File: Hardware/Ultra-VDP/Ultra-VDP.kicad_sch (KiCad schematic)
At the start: 70 parts, among them J1 BC075-05, J2 BC075-10, J3 CBUS, J4 BC075-10, J5 BC075-06, J6 BC075-10, J7 BC075-10, J8 BC075-05, U14 V53C8125HT30, U3 V9958, U6 LMH1980, Y1 21.477270MHz, Y3 4.433618MHz

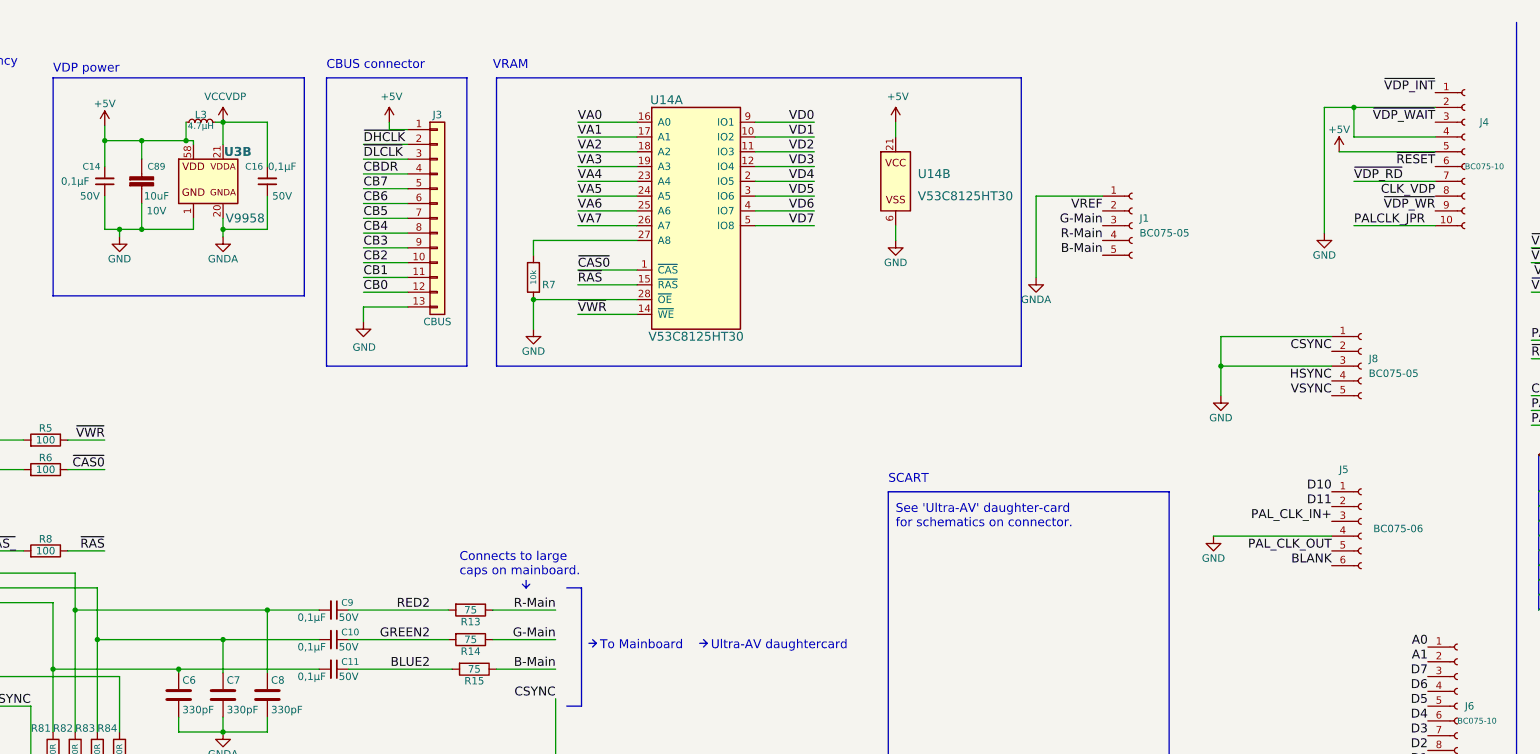
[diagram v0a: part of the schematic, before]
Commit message: Finished the VDP-board, finished up the mixer-section, removed the buffer-pins from the FPGA, and instead added external buffers for the slots, designed a marquee-block with the Ultra-MSX logo, designed the logotype, andmultiple other changes.
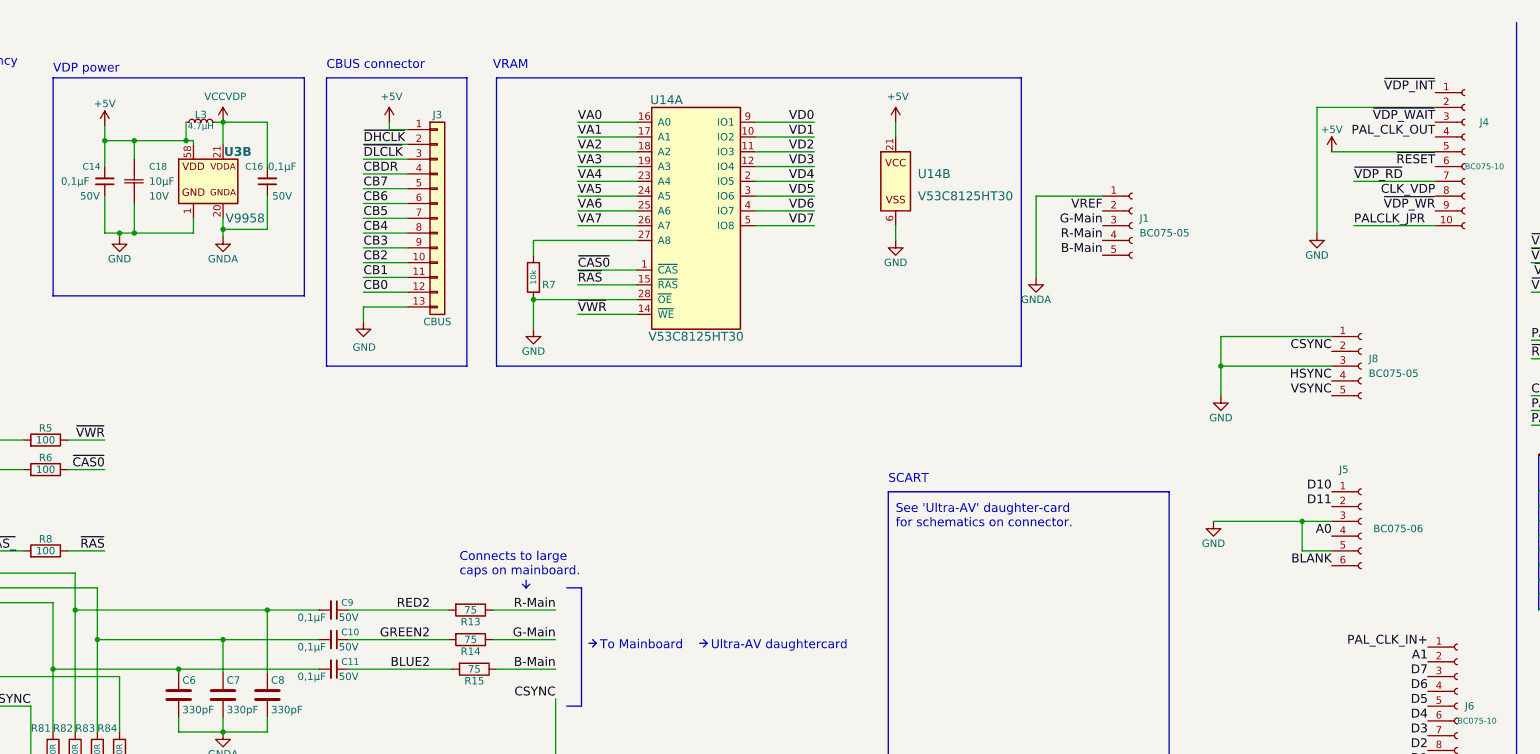
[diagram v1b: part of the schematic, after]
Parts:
- removed C89: C_GRM21BR71A106KA73K, Capacitor_SMD:C_0805_2012Metric_Pad1.18x1.45mm_HandSolder, symbol LRJ-parts:C_GRM21BR71A106KA73K
- added C18: C_GRM188D71A106KA73D, Capacitor_SMD:C_0603_1608Metric, symbol LRJ-parts:C_GRM188D71A106KA73D
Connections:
- net +5V: now also C18.1
- net A0: now also J5.4 (Pin_4); no longer J6.1 (Pin_1)
- net GND: now also J5.3 (Pin_3), J5.5 (Pin_5), C18.2; no longer J4.4 (Pin_4), J5.4 (Pin_4)
- net PAL_CLK_IN+: now also J6.1 (Pin_1); no longer J5.3 (Pin_3)
- net PAL_CLK_OUT: now also J4.4 (Pin_4); no longer J5.5 (Pin_5)

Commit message: Redesigned VDP-board to include a socket, increased it to 4 layers. Various clean-ups here and there. Improved the printer-port and joystick-port 3D-models. Improved the cooling-fin 3D-model, and added attachment-spring in 3D-model.
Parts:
- removed C3: 0.1uF, Capacitor_SMD:C_0603_1608Metric, symbol Device:C
- added C19: 47pF, Capacitor_SMD:C_0603_1608Metric, symbol Device:C
- added C3: C_CL21B223KBANFNC, Capacitor_SMD:C_0805_2012Metric_Pad1.18x1.45mm_HandSolder, symbol LRJ-parts:C_CL21B223KBANFNC
- added L1: L_MLZ2012M4R7HT000, Inductor_SMD:L_0805_2012Metric, symbol LRJ-parts:L_MLZ2012M4R7HT000
- added R10: 75, Resistor_SMD:R_0603_1608Metric, symbol Device:R
- added R12: 100, Resistor_SMD:R_0603_1608Metric, symbol Device:R
- U3: footprint Ultra-MSX:IC_SDIP64_600 -> Ultra-MSX:DIP-64_W19.05mm_SMDSocket_SmallPads
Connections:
- net +5V: now also R20.1, L1.1; no longer C17.1, C73.1, R20.2, R60.2, U6.3 (VCC)
- net COMPSYNC: now also R10.1, R12.2; no longer C12.1, C15.2
- net GND: now also C19.2, C3.2, R10.2
- net VCCVDP: now also R60.2
- net ~{VDP_INT}: now also R20.2; no longer R20.1
- net HORSYNC: now reaches R84.1, U3.5 (HSYNC)
- net PALCLK_JPR renamed NTSC_CLKO
- new net: C12.1, C15.2, C19.1, R12.1
- new net: C3.1, U3.33 (VBB)
- new net +5V_SYNC: C17.1, C73.1, L1.2, U6.3 (VCC)
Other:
- note added: "1. Video Display Processor (VDP)"
- note added: "1.1. VDP power"
- note added: "1.2. CBUS connector"
- note added: "1/6 of Crystal Frequency (3,579545 MHz, aka NTSC)"
- note added: "2. VRAM"
- note added: "DisplayPort has a mode where it sends raw RGB down the wire, meaning a DP to VGA converter is "just" a DAC and maybe a presence detection EEPROM. Example-chip:"
- note added: "From the MSX-Engine (see Mainboard)"
- note added: "PCB Layout Notes: DIP-64 socket - Mill-Max 117-43-764-41-105000"
- note added: "VGA clocks: ------------- 640x400 (70Hz) - 25.175 MHz 640x480 (60Hz) - 25.175 MHz Pal clocks: ------------- 704x576 (50Hz) - 4.43361875 MHz NTSC clocks: -------------- 704x480 (60Hz) - 3.579545 MHz"
- note removed: "1/6 of Crystal Frequency (3,579545 MHz)"
- note removed: "CBUS connector"
- note removed: "DisplayPort has a mode where it sends raw RGB down the wire, meaning a DP to VGA converter is "just" a DAC and maybe a presence detection EEPROM. Example-chip: PTN3356R1BSMP"
- note removed: "PCB Layout Notes: Keep trace length between AD723 and 75 ohm resistors to minimum AD723 bypass capacitors: VCC1(12), VREF(14) -> GND1(1), VCC2(19) -> GND2(24)"
- note removed: "VCC_ROM"
- note removed: "VDP power"
- note removed: "VRAM"
- moved on the sheet: C1, C10, C11, C12, C13, C14, C15, C16, C17, C18, C2, C4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

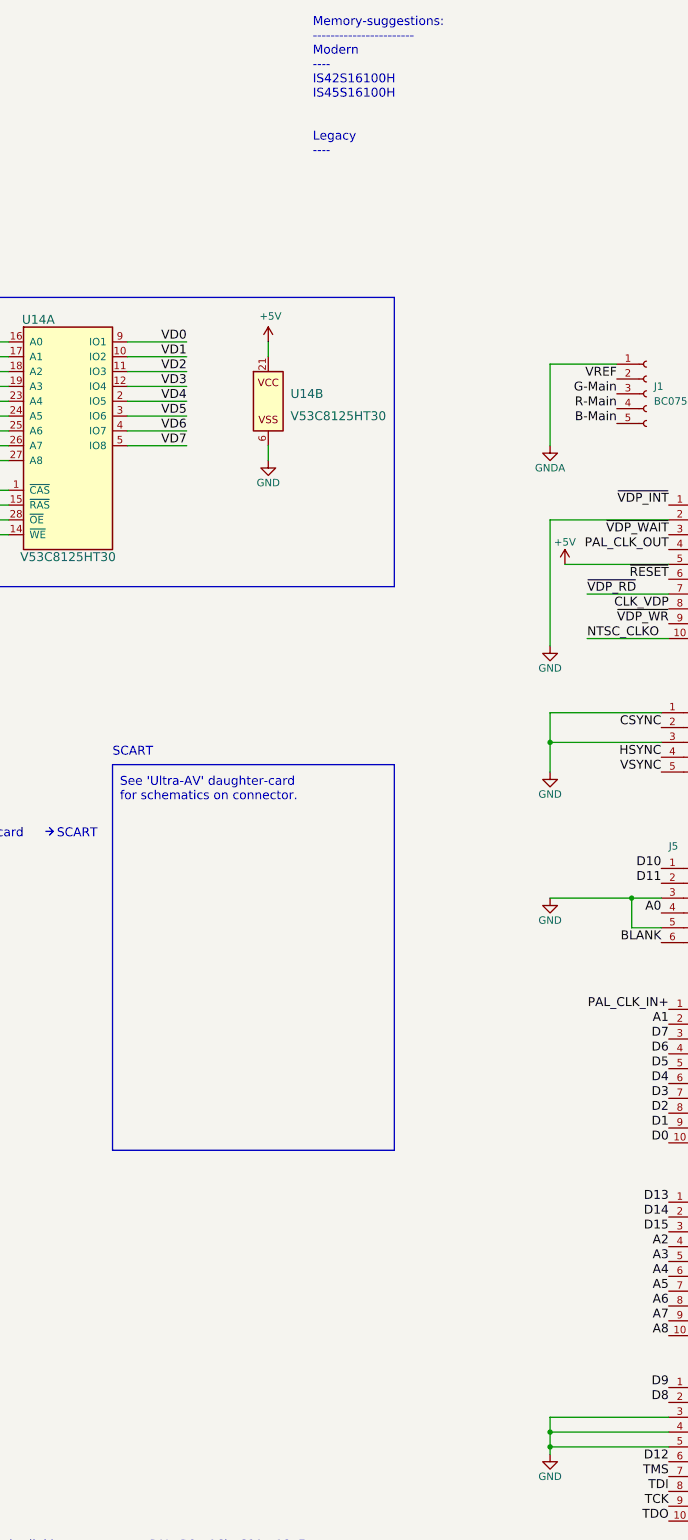
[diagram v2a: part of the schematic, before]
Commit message: Generated first PDF-files
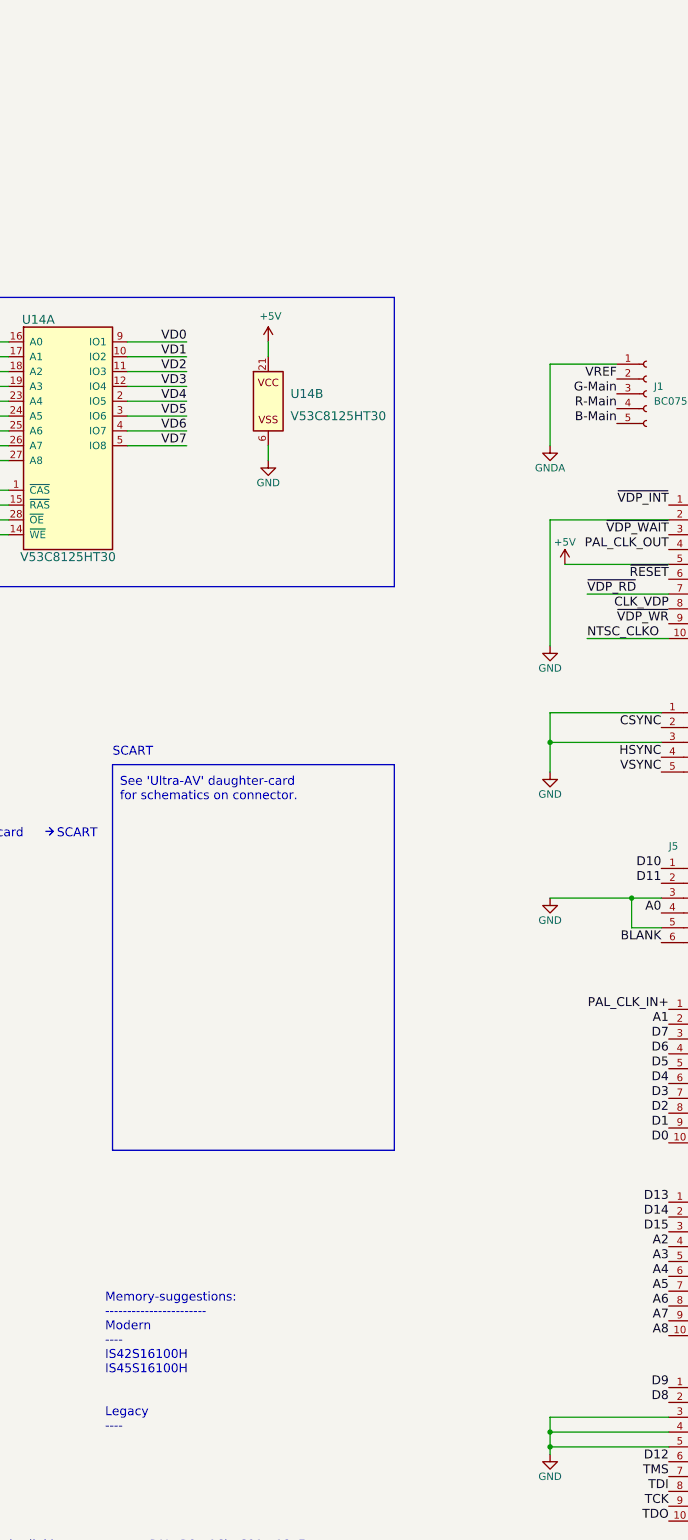
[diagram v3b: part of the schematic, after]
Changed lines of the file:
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@@
   )
   (text "Memory-suggestions:\n-----------------------\nModern\n----\nIS42S16100H\nIS45S16100H\n\n\nLegacy\n----"
-    (at 299.72 -5.08 0)
+    (at 264.16 213.36 0)
     (effects (font (size 1.524 1.524)) (justify left bottom))
   )

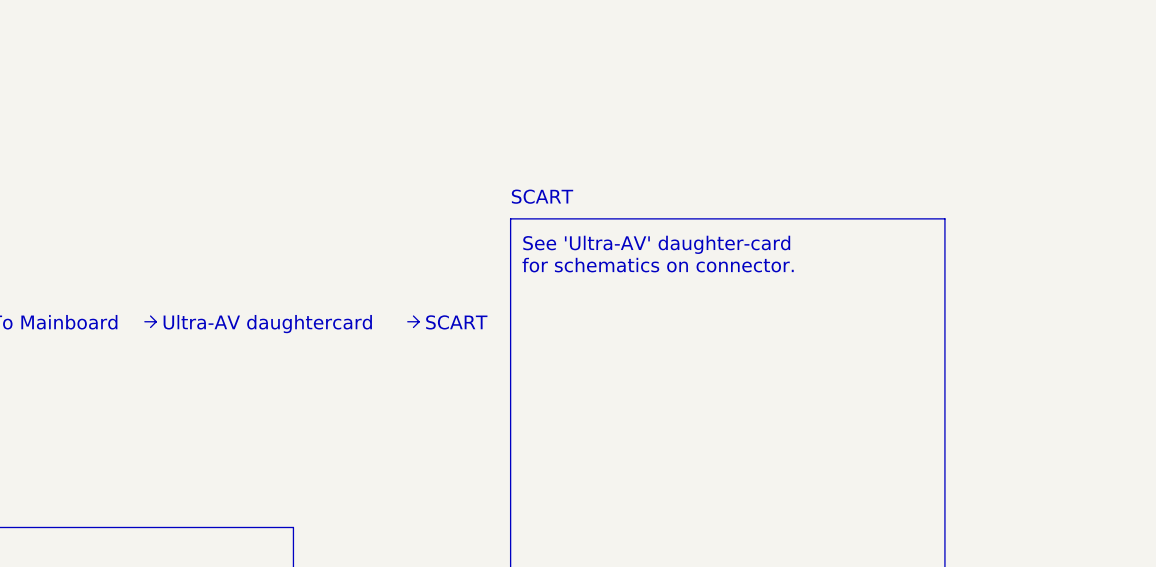
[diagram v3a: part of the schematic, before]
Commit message: Started remodelling the MSX cart-shells, as they don't seem to fit the cartridge-pcb's. Bit of clean-up in the directories.
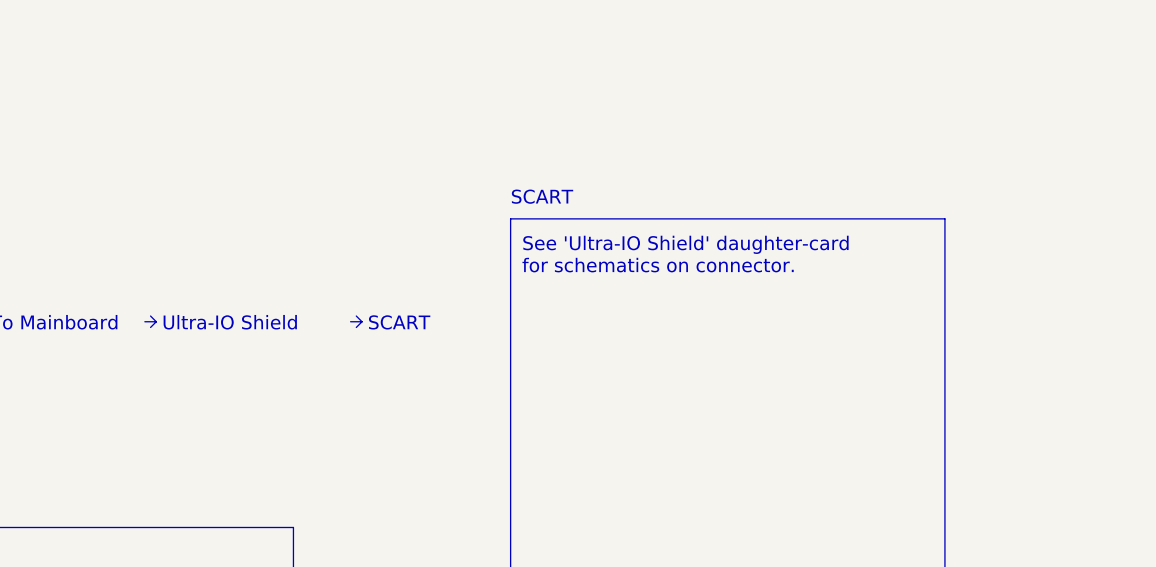
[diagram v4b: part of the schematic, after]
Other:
- note added: "See 'Ultra-IO Shield' daughter-card for schematics on connector."
- note added: "Ultra-IO Shield"
- note removed: "See 'Ultra-AV' daughter-card for schematics on connector."
- note removed: "Ultra-AV daughtercard"
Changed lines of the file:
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@@
     (stroke (width 0) (type default) (color 0 0 0 0))
   )
-  (polyline (pts (xy 254 110.49) (xy 255.27 110.49))
+  (polyline (pts (xy 247.65 110.49) (xy 248.92 110.49))
     (stroke (width 0) (type solid) (color 0 0 0 0))
   )
@@
     (stroke (width 0) (type default) (color 0 0 0 0))
   )
-  (polyline (pts (xy 254.635 111.125) (xy 255.27 110.49))
+  (polyline (pts (xy 248.285 111.125) (xy 248.92 110.49))
     (stroke (width 0) (type solid) (color 0 0 0 0))
   )
@@
     (stroke (width 0) (type default) (color 0 0 0 0))
   )
-  (polyline (pts (xy 254.635 109.855) (xy 255.27 110.49))
+  (polyline (pts (xy 248.285 109.855) (xy 248.92 110.49))
     (stroke (width 0) (type solid) (color 0 0 0 0))
   )
@@
     (effects (font (size 1.524 1.524)) (justify left bottom))
   )
-  (text "See 'Ultra-AV' daughter-card \nfor schematics on connector."
+  (text "See 'Ultra-IO Shield' daughter-card \nfor schematics on connector."
     (at 266.7 105.41 0)
     (effects (font (size 1.524 1.524)) (justify left bottom))
@@
     (effects (font (size 1.524 1.524)) (justify left bottom))
   )
-  (text "Ultra-AV daughtercard\n" (at 226.695 111.76 0)
+  (text "Ultra-IO Shield\n" (at 226.695 111.76 0)
     (effects (font (size 1.524 1.524)) (justify left bottom))
   )
@@
     (effects (font (size 1.524 1.524)) (justify left bottom))
   )
-  (text "SCART\n" (at 255.905 111.76 0)
+  (text "SCART\n" (at 249.555 111.76 0)
     (effects (font (size 1.524 1.524)) (justify left bottom))
   )

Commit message: Started fixing many small issues.
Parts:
- added trace1, trace10, trace11, trace12, trace13, trace14, trace15, trace16, trace17, trace18, trace19, trace2, trace20, trace21, trace3, trace4, trace5, trace6, trace7, trace8, trace9: pcb-trace, LRJ:NetTie-2_SMD_Pad0.2mm, symbol LRJ-parts:Trace
- C10, C11, C14, C15, C16, C17, C9: Mounting Type SMD -> (none); Mounting type (none) -> SMD; Voltage Rating (none) -> 50V; Voltage Rating  50V -> (none)
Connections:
- net GNDA is gone; now on net GND: C16.1, C6.2, C7.2, C8.2, J1.1 (Pin_1), R81.2, R82.2, R83.2, U3.20 (GNDA)
- net +5V: now also C73.1
- net A2: now also trace5.2
- net A3: now also trace6.2
- net A4: now also trace7.2
- net A5: now also trace8.2
- net A6: now also trace9.2
- net A7: now also trace10.2
- net A8: now also trace11.2
- net BLANK: now also trace21.1; no longer J5.6 (Pin_6)
- net D10: now also trace19.1
- net D11: now also trace20.1
- net D12: now also trace14.2
- net D13: now also trace1.2
- net D14: now also trace3.2
- net D15: now also trace4.2
- net D8: now also trace13.2
- net D9: now also trace12.2
- net TCK: now also trace17.2
- net TDI: now also trace16.2
- net TDO: now also trace18.2
- net TMS: now also trace15.2
- net VREF: now also trace2.2
- net +5V_SYNC renamed VDDSYNC
- net VDDSYNC: no longer C73.1
- new net: J5.6 (Pin_6), trace21.2
- no-connect marks 3 -> 24
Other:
- note added: "2. Video Random Access Memory (VRAM)"
- note added: "3. Sync Separator"
- note added: "3.1. Sync Separator power"
- note added: "4. PAL Clock Generator"
- note added: "4.1. Region Selection"
- note added: "5. SCART Connector"
- note added: "6. Motherboard connectors"
- note added: "Addressing"
- note added: "CLOCK signals"
- note added: "CONTROL signals"
- note added: "DATA bus"
- note added: "JP4, JP5: 1-2: NTSC; 2-3: PAL (Use a wire link)"
- note added: "Note: these pins are only in use when utilizing a more advanced VDP such as V9990, or F18A. ->"
- note added: "To Motherboard"
- note added: "VIDEO signals"
- note added: "up to: 56 pins. But we can shave it down to 51... Potential sockets: Amphenol FCI MDT350M01001VT (M.2) Samtec PCIE-LP-04-01-F-DV-A-TR (PCIe x4)"
- note removed: "2. VRAM"
- note removed: "JP3, JP4: 1-2: V9938; 2-3: V9958 (Use a wire link) JP4, JP5: 1-2: NTSC; 2-3: PAL (Use a wire link)"
- note removed: "PAL Clock Generator"
- note removed: "Sync Separator power"
- note removed: "To Mainboard"
- title: (none) -> Ultra-VDP
- moved on the sheet: C1, C10, C11, C12, C13, C14, C15, C16, C17, C18, C19, C2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
